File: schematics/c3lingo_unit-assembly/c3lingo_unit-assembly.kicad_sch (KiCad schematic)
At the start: 0 parts

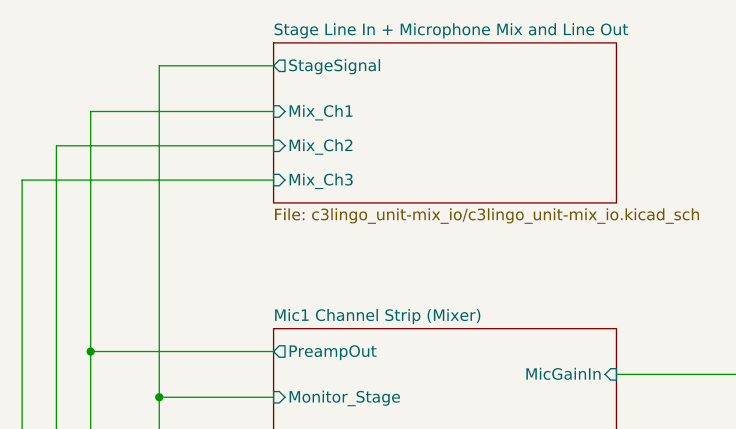
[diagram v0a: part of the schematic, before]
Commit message: Reworks board-to-board connections
Instead of having connections between all boards, use the mix_io board as an audio signal distribution hub.

Note: PCB not updated
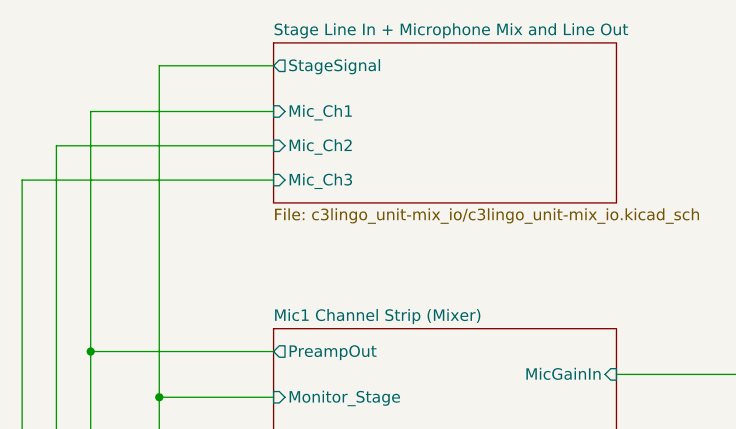
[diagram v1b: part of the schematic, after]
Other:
- sheet Stage Line In + Microphone Mix and Line Out ports: added Mic_Ch1, Mic_Ch2, Mic_Ch3; removed Mix_Ch1, Mix_Ch2, Mix_Ch3
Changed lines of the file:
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@@
 	(title_block
 		(title "c3lingo interpeter unit")
-		(date "2024-03-04")
+		(date "2024-06-30")
 		(rev "v0.3.0")
 		(company "Jannik Beyerstedt (jtbx)")
@@
 			)
 		)
-		(pin "Mix_Ch1" input
+		(pin "Mic_Ch1" input
 			(at 127 33.02 180)
 			(effects
@@
 			)
 		)
-		(pin "Mix_Ch2" input
+		(pin "Mic_Ch2" input
 			(at 127 36.83 180)
 			(effects
@@
 			)
 		)
-		(pin "Mix_Ch3" input
+		(pin "Mic_Ch3" input
 			(at 127 40.64 180)
 			(effects

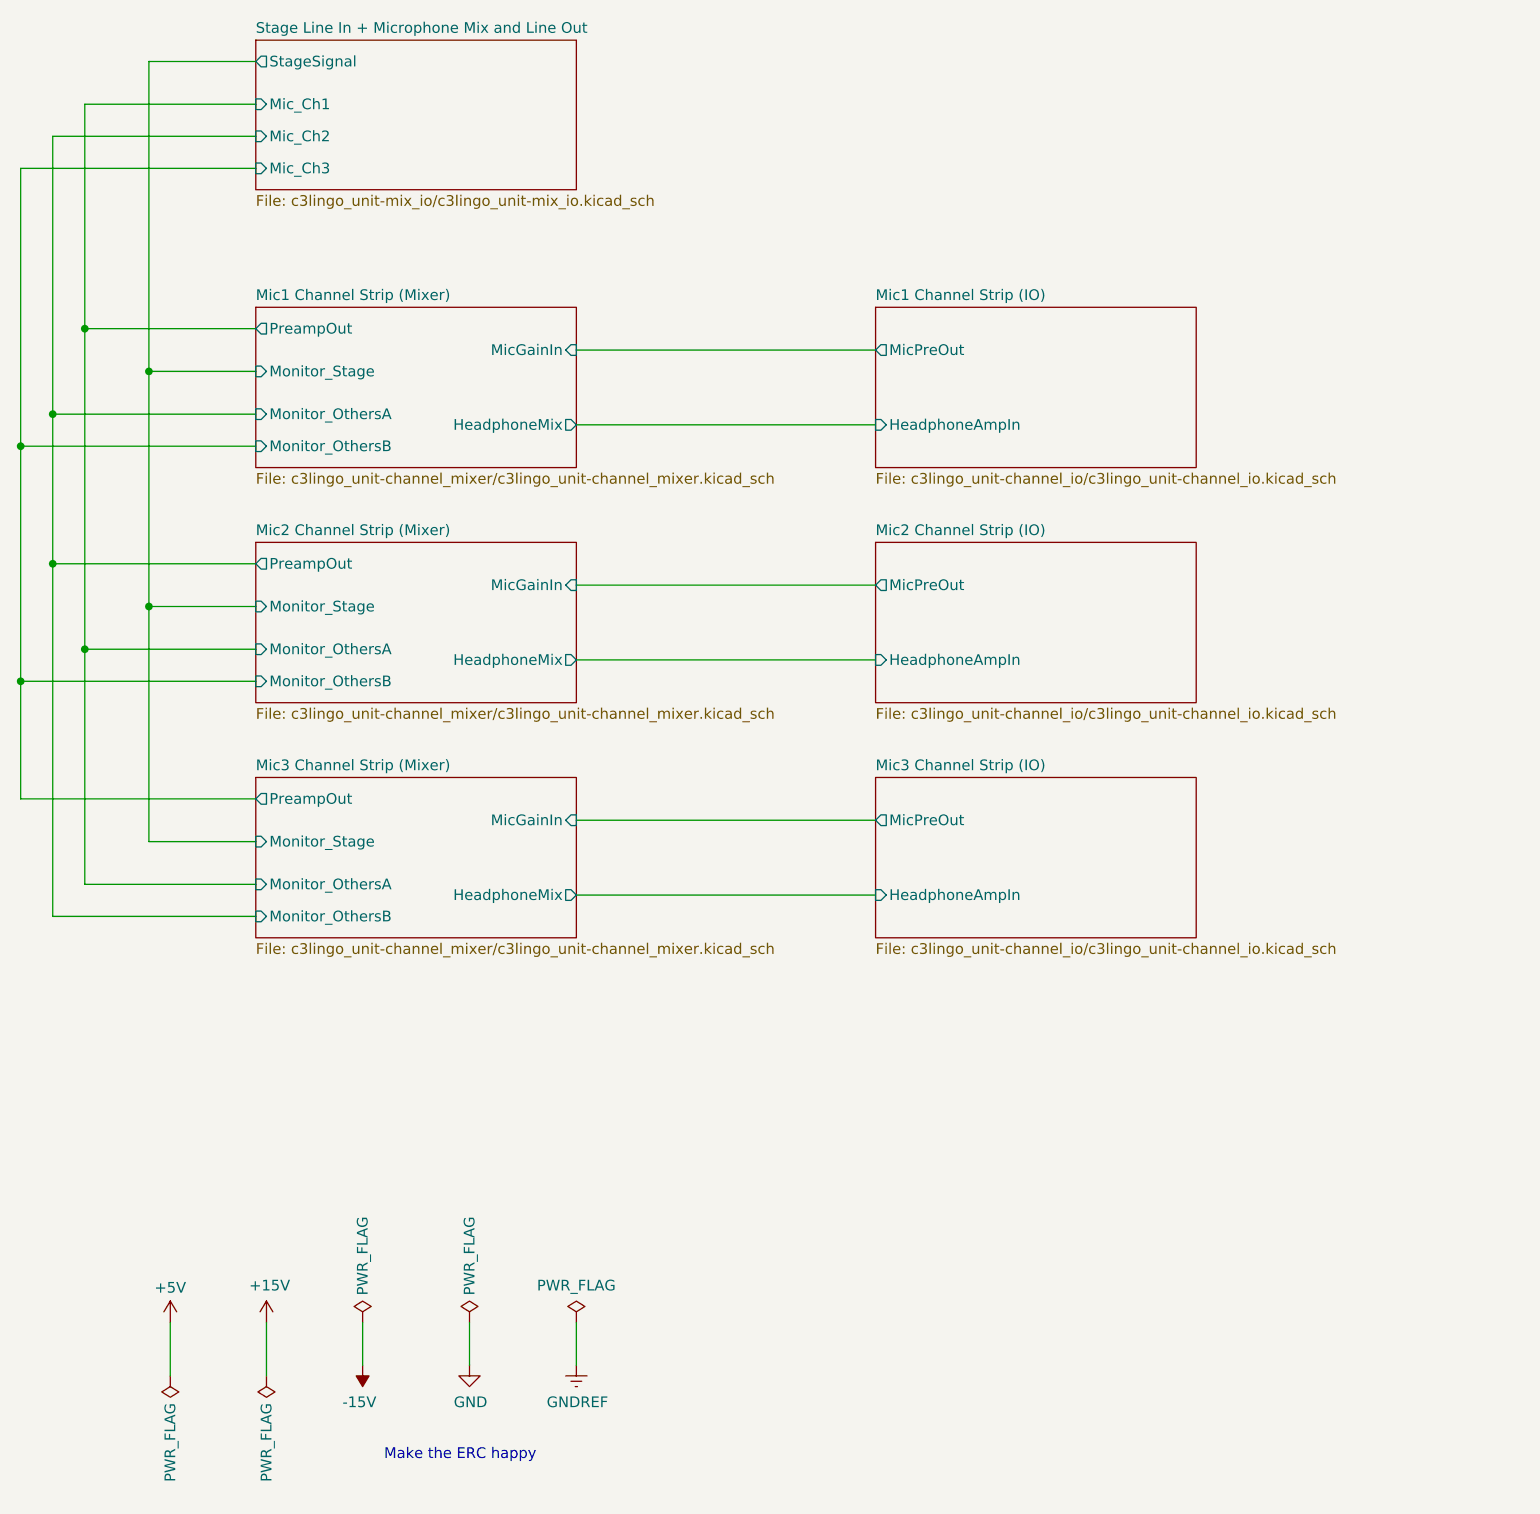
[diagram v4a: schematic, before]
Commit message: Tidy: Rename hierarchical labels
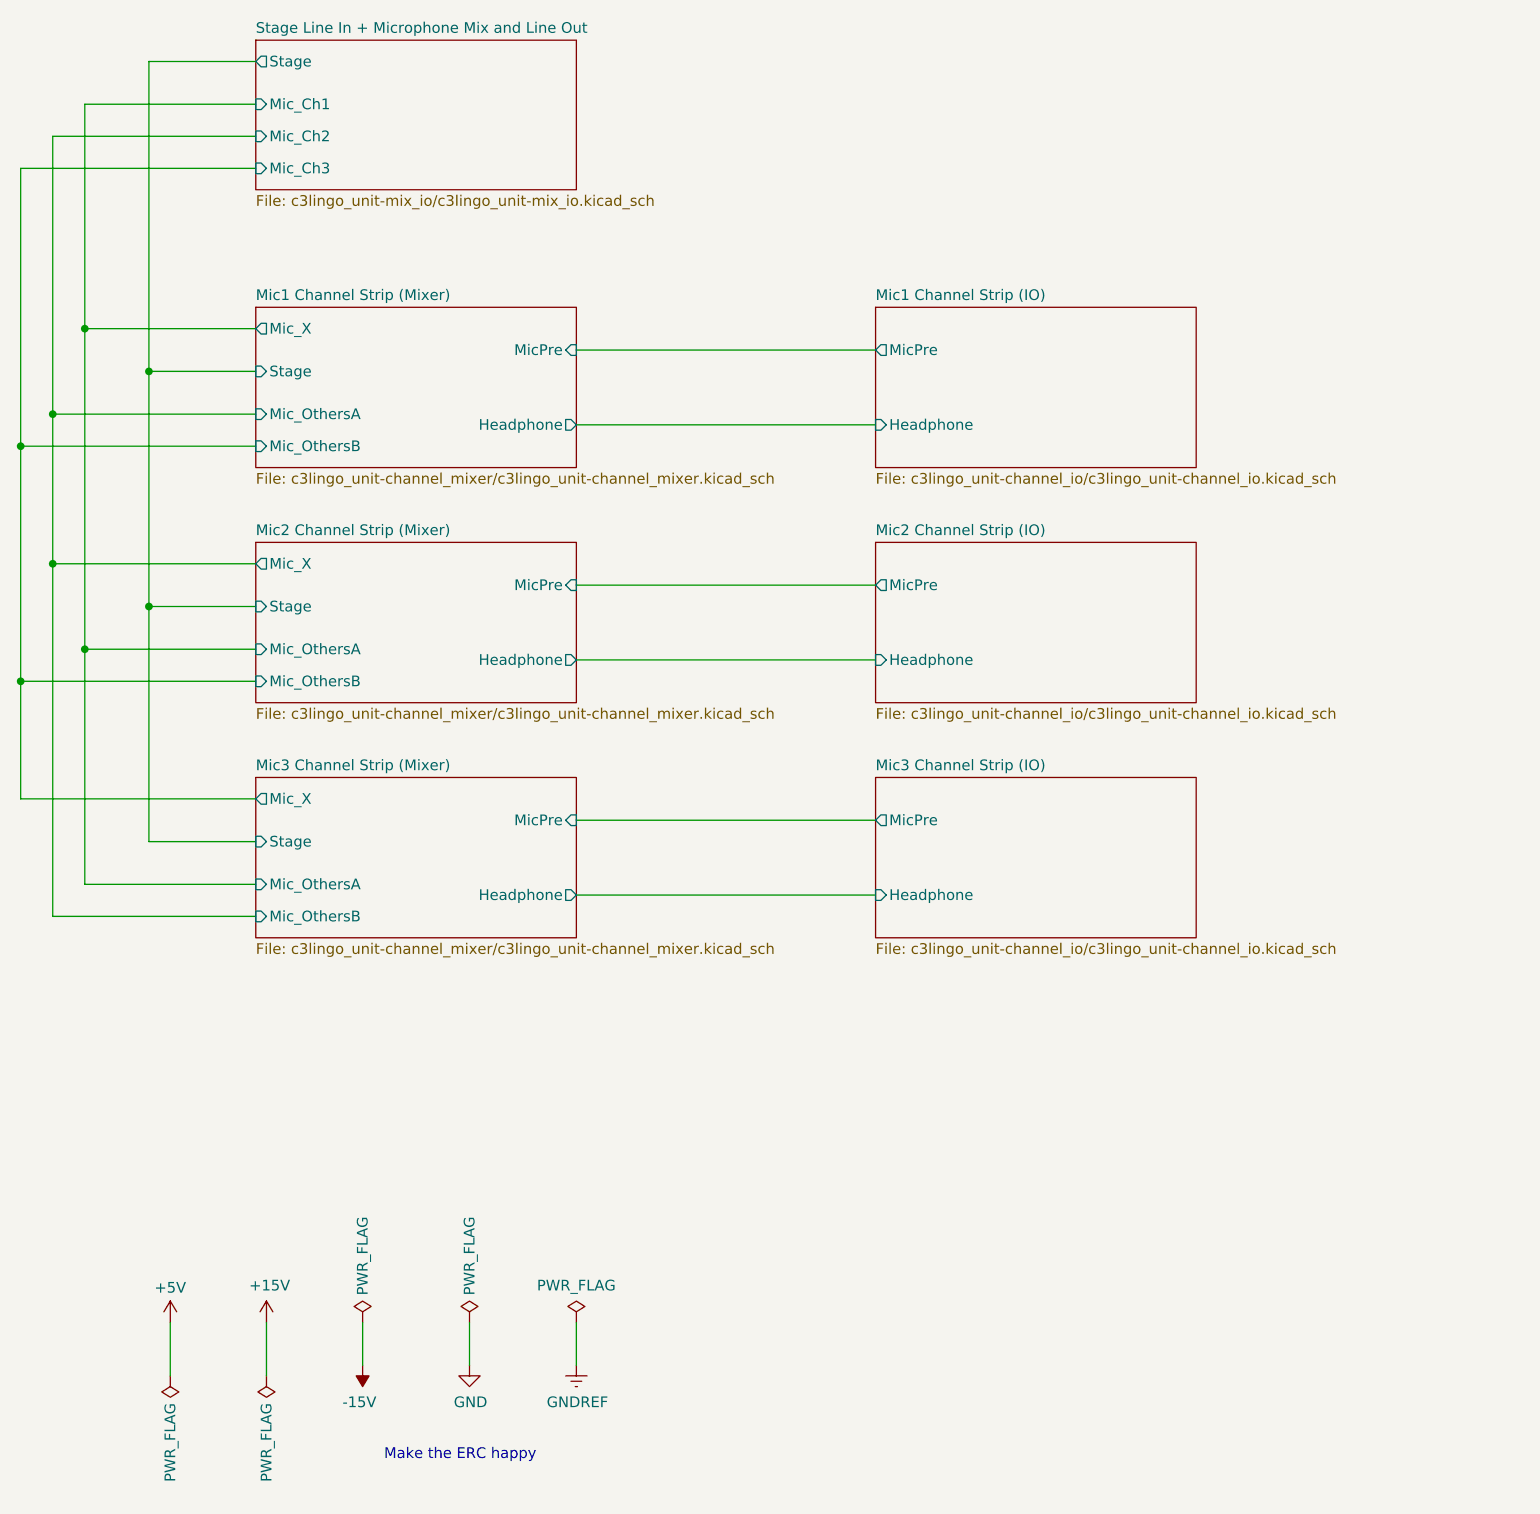
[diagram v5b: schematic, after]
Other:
- sheet Mic1 Channel Strip (IO) ports: added Headphone, MicPre; removed HeadphoneAmpIn, MicPreOut
- sheet Mic1 Channel Strip (Mixer) ports: added Headphone, MicPre, Mic_OthersA, Mic_OthersB, Mic_X, Stage; removed HeadphoneMix, MicGainIn, Monitor_OthersA, Monitor_OthersB, Monitor_Stage, PreampOut
- sheet Mic2 Channel Strip (IO) ports: added Headphone, MicPre; removed HeadphoneAmpIn, MicPreOut
- sheet Mic2 Channel Strip (Mixer) ports: added Headphone, MicPre, Mic_OthersA, Mic_OthersB, Mic_X, Stage; removed HeadphoneMix, MicGainIn, Monitor_OthersA, Monitor_OthersB, Monitor_Stage, PreampOut
- sheet Mic3 Channel Strip (IO) ports: added Headphone, MicPre; removed HeadphoneAmpIn, MicPreOut
- sheet Mic3 Channel Strip (Mixer) ports: added Headphone, MicPre, Mic_OthersA, Mic_OthersB, Mic_X, Stage; removed HeadphoneMix, MicGainIn, Monitor_OthersA, Monitor_OthersB, Monitor_Stage, PreampOut
- sheet Stage Line In + Microphone Mix and Line Out ports: added Stage; removed StageSignal
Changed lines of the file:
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@@
 			)
 		)
-		(pin "PreampOut" output
+		(pin "Mic_X" output
 			(at 127 59.69 180)
 			(effects
@@
 			)
 		)
-		(pin "Monitor_OthersA" input
+		(pin "Mic_OthersA" input
 			(at 127 69.85 180)
 			(effects
@@
 			)
 		)
-		(pin "Monitor_OthersB" input
+		(pin "Mic_OthersB" input
 			(at 127 73.66 180)
 			(effects
@@
 			)
 		)
-		(pin "Monitor_Stage" input
+		(pin "Stage" input
 			(at 127 64.77 180)
 			(effects
@@
 			)
 		)
-		(pin "MicGainIn" input
+		(pin "MicPre" input
 			(at 165.1 62.23 0)
 			(effects
@@
 			)
 		)
-		(pin "HeadphoneMix" output
+		(pin "Headphone" output
 			(at 165.1 71.12 0)
 			(effects
@@
 			)
 		)
-		(pin "StageSignal" output
+		(pin "Stage" output
 			(at 127 27.94 180)
 			(effects
@@
 			)
 		)
-		(pin "PreampOut" output
+		(pin "Mic_X" output
 			(at 127 87.63 180)
 			(effects
@@
 			)
 		)
-		(pin "Monitor_OthersA" input
+		(pin "Mic_OthersA" input
 			(at 127 97.79 180)
 			(effects
@@
 			)
 		)
-		(pin "Monitor_OthersB" input
+		(pin "Mic_OthersB" input
 			(at 127 101.6 180)
 			(effects
@@
 			)
 		)
-		(pin "Monitor_Stage" input
+		(pin "Stage" input
 			(at 127 92.71 180)
 			(effects
@@
 			)
 		)
-		(pin "MicGainIn" input
+		(pin "MicPre" input
 			(at 165.1 90.17 0)
 			(effects
@@
 			)
 		)
-		(pin "HeadphoneMix" output
+		(pin "Headphone" output
 			(at 165.1 99.06 0)
 			(effects
@@
 			)
 		)
-		(pin "PreampOut" output
+		(pin "Mic_X" output
 			(at 127 115.57 180)
 			(effects
@@
 			)
 		)
-		(pin "Monitor_OthersA" input
+		(pin "Mic_OthersA" input
 			(at 127 125.73 180)
 			(effects
@@
 			)
 		)
-		(pin "Monitor_OthersB" input
+		(pin "Mic_OthersB" input
 			(at 127 129.54 180)
 			(effects
@@
 			)
 		)
-		(pin "Monitor_Stage" input
+		(pin "Stage" input
 			(at 127 120.65 180)
 			(effects
@@
 			)
 		)
-		(pin "MicGainIn" input
+		(pin "MicPre" input
 			(at 165.1 118.11 0)
 			(effects
@@
 			)
 		)
-		(pin "HeadphoneMix" output
+		(pin "Headphone" output
 			(at 165.1 127 0)
 			(effects
@@
 			)
 		)
-		(pin "MicPreOut" output
+		(pin "MicPre" output
 			(at 200.66 118.11 180)
 			(effects
@@
 			)
 		)
-		(pin "HeadphoneAmpIn" input
+		(pin "Headphone" input
 			(at 200.66 127 180)
 			(effects
@@
 			)
 		)
-		(pin "MicPreOut" output
+		(pin "MicPre" output
 			(at 200.66 62.23 180)
 			(effects
@@
 			)
 		)
-		(pin "HeadphoneAmpIn" input
+		(pin "Headphone" input
 			(at 200.66 71.12 180)
 			(effects
@@
 			)
 		)
-		(pin "MicPreOut" output
+		(pin "MicPre" output
 			(at 200.66 90.17 180)
 			(effects
@@
 			)
 		)
-		(pin "HeadphoneAmpIn" input
+		(pin "Headphone" input
 			(at 200.66 99.06 180)
 			(effects
